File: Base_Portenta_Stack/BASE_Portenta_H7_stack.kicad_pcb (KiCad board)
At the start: 2 copper layers, 79.8 x 26.6 mm, 8 parts, among them J4 PinHeader_1x04_P2.00mm_Vertic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

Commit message: Updade
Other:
- outline, holes or cut-outs redrawn
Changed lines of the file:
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@@
       )
     )
-    (model "${KIPRJMOD}/Arduino-Portenta-H7-STEP-A210428.step"
+    (model "C:/Users/45262/Documents/GitHub/MTBeDRIVE/img/DF40C(2.0)-80DS.stp"
+      (offset (xyz 0.1 15.9 0.5))
+      (scale (xyz 1 1 1))
+      (rotate (xyz 90 -180 90))
+    )
+    (model "C:/Users/45262/Documents/GitHub/MTBeDRIVE/img/DF40C(2.0)-80DS.stp"
+      (offset (xyz -0.1 -27.3 0.5))
+      (scale (xyz 1 1 1))
+      (rotate (xyz -90 0 90))
+    )
+    (model "C:/Users/45262/Desktop/NRF_HALLA/Arduino-Portenta-H7-STEP-A210428.step"
       (offset (xyz 0 0 2))
       (scale (xyz 1 1 1))
@@
     )
   )
-  (gr_rect (start 106.21 80.47) (end 185.98 107.09) (layer "Edge.Cuts") (width 0.05) (fill none))
+  (gr_arc (start 183.950563 80.472791) (mid 185.42 80.95) (end 185.960563 82.392791) (layer "Edge.Cuts") (width 0.05))
+  (gr_line (start 184.047772 107.093354) (end 108.22 107.09) (layer "Edge.Cuts") (width 0.1))
+  (gr_arc (start 185.967772 105.083354) (mid 185.490563 106.552791) (end 184.047772 107.093354) (layer "Edge.Cuts") (width 0.05))
+  (gr_arc (start 108.22 107.09) (mid 106.750563 106.612791) (end 106.21 105.17) (layer "Edge.Cuts") (width 0.05))
+  (gr_line (start 108.122791 80.469437) (end 183.950563 80.472791) (layer "Edge.Cuts") (width 0.1))
+  (gr_arc (start 106.202791 82.479437) (mid 106.68 81.01) (end 108.122791 80.469437) (layer "Edge.Cuts") (width 0.05))
+  (gr_line (start 106.21 105.17) (end 106.202791 82.479437) (layer "Edge.Cuts") (width 0.1))
+  (gr_line (start 185.960563 82.392791) (end 185.967772 105.083354) (layer "Edge.Cuts") (width 0.1))
 )

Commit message: Log
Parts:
- added REF**: VSON-10-1EP_3x3mm_P0.5mm_EP1.2x2mm, Package_SON:VSON-10-1EP_3x3mm_P0.5mm_EP1.2x2mm, B.Cu at (167.6, 93.7)
- added REF**: D_1206_3216Metric, Diode_SMD:D_1206_3216Metric, B.Cu at (175.8, 93.6)
- added REF**: C_0805_2012Metric, Capacitor_SMD:C_0805_2012Metric, B.Cu at (181.6, 100.1)
- added REF**: C_1210_3225Metric, Capacitor_SMD:C_1210_3225Metric, B.Cu at (181.3, 86.3)
- added REF**: MountingHole_3.2mm_M3, MountingHole:MountingHole_3.2mm_M3, F.Cu at (182.2, 93.4)
- added REF**: MountingHole_3.2mm_M3, MountingHole:MountingHole_3.2mm_M3, F.Cu at (110.4, 93.4)
- added REF**: C_0805_2012Metric, Capacitor_SMD:C_0805_2012Metric, B.Cu at (171.4, 93.7)
- added REF**: SRP5050, MAX40056FAWA&plus_:SRP5050, B.Cu at (176.1, 98.1)
- added REF**: SOIC-8_EP_MNP, MP9486AGN-Z:MP9486AGN-Z, B.Cu at (176.1, 88.2)
- added REF**: C_1210_3225Metric, Capacitor_SMD:C_1210_3225Metric, B.Cu at (181.3, 82.9)
- added REF**: CP_EIA-7343-15_Kemet-W, Capacitor_Tantalum_SMD:CP_EIA-7343-15_Kemet-W, B.Cu at (178.7, 103.9)
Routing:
- added copper zone on B.Cu, net GND
- added copper zone on B.Cu, net SW
- added copper zone on B.Cu, net SWT_OUT_12V
- added copper zone on B.Cu, net VIN

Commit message: Update BASE_Portenta_H7_stack.kicad_pcb
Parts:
- removed the REF** at (110.4, 93.4)
- added REF**: PinHeader_1x04_P2.54mm_Vertical, Connector_PinHeader_2.54mm:PinHeader_1x04_P2.54mm_Vertical, F.Cu at (100.9, 97.5)
- added REF**: R_0603_1608Metric, Resistor_SMD:R_0603_1608Metric, B.Cu at (173.9, 82.0)
- added REF**: R_0603_1608Metric, Resistor_SMD:R_0603_1608Metric, B.Cu at (175.4, 82.0)
- added REF**: C_0603_1608Metric, Capacitor_SMD:C_0603_1608Metric, B.Cu at (176.9, 82.0)
- added REF**: PinHeader_1x06_P2.00mm_Vertical, Connector_PinHeader_2.00mm:PinHeader_1x06_P2.00mm_Vertical, F.Cu at (100.8, 82.5)
- REF**: moved to F.Cu
- U1: renamed from REF**; value MODULE_ABX00042 -> ABX00042
- moved REF** 0.51 mm to (181.7, 86.7)
- moved REF** 0.32 mm to (181.6, 83.0)
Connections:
- U1 pad J1_1: (no net) -> unconnected-(U1-PadJ1_1)
- U1 pad J1_10: (no net) -> unconnected-(U1-PadJ1_10)
- U1 pad J1_11: (no net) -> unconnected-(U1-PadJ1_11)
- U1 pad J1_12: (no net) -> unconnected-(U1-PadJ1_12)
- U1 pad J1_13: (no net) -> unconnected-(U1-PadJ1_13)
- U1 pad J1_14: (no net) -> unconnected-(U1-PadJ1_14)
- U1 pad J1_15: (no net) -> unconnected-(U1-PadJ1_15)
- U1 pad J1_16: (no net) -> unconnected-(U1-PadJ1_16)
- U1 pad J1_17: (no net) -> unconnected-(U1-PadJ1_17)
- U1 pad J1_18: (no net) -> unconnected-(U1-PadJ1_18)
- U1 pad J1_19: (no net) -> unconnected-(U1-PadJ1_19)
- U1 pad J1_2: (no net) -> unconnected-(U1-PadJ1_2)
- U1 pad J1_20: (no net) -> unconnected-(U1-PadJ1_20)
- U1 pad J1_21: (no net) -> Net-(U1-PadJ1_21)
- U1 pad J1_22: (no net) -> Net-(U1-PadJ1_22)
- U1 pad J1_23: (no net) -> unconnected-(U1-PadJ1_23)
- U1 pad J1_24: (no net) -> unconnected-(U1-PadJ1_24)
- U1 pad J1_25: (no net) -> unconnected-(U1-PadJ1_25)
- U1 pad J1_26: (no net) -> unconnected-(U1-PadJ1_26)
- U1 pad J1_27: (no net) -> unconnected-(U1-PadJ1_27)
- U1 pad J1_28: (no net) -> unconnected-(U1-PadJ1_28)
- U1 pad J1_29: (no net) -> unconnected-(U1-PadJ1_29)
- U1 pad J1_3: (no net) -> unconnected-(U1-PadJ1_3)
- U1 pad J1_30: (no net) -> unconnected-(U1-PadJ1_30)
- U1 pad J1_31: (no net) -> Net-(U1-PadJ1_22)
- U1 pad J1_32: (no net) -> Net-(U1-PadJ1_21)
- U1 pad J1_33: (no net) -> unconnected-(U1-PadJ1_33)
- U1 pad J1_34: (no net) -> unconnected-(U1-PadJ1_34)
- U1 pad J1_35: (no net) -> unconnected-(U1-PadJ1_35)
- U1 pad J1_36: (no net) -> unconnected-(U1-PadJ1_36)
- U1 pad J1_37: (no net) -> unconnected-(U1-PadJ1_37)
- U1 pad J1_38: (no net) -> unconnected-(U1-PadJ1_38)
- U1 pad J1_39: (no net) -> unconnected-(U1-PadJ1_39)
- U1 pad J1_4: (no net) -> unconnected-(U1-PadJ1_4)
- U1 pad J1_40: (no net) -> unconnected-(U1-PadJ1_40)
- U1 pad J1_41: (no net) -> Net-(U1-PadJ1_21)
- U1 pad J1_42: (no net) -> Net-(U1-PadJ1_22)
- U1 pad J1_43: (no net) -> unconnected-(U1-PadJ1_43)
- U1 pad J1_44: (no net) -> unconnected-(U1-PadJ1_44)
- U1 pad J1_45: (no net) -> unconnected-(U1-PadJ1_45)
- U1 pad J1_46: (no net) -> unconnected-(U1-PadJ1_46)
- U1 pad J1_47: (no net) -> Net-(U1-PadJ1_22)
- U1 pad J1_48: (no net) -> Net-(U1-PadJ1_21)
- U1 pad J1_49: (no net) -> unconnected-(U1-PadJ1_49)
- U1 pad J1_5: (no net) -> unconnected-(U1-PadJ1_5)
- U1 pad J1_50: (no net) -> unconnected-(U1-PadJ1_50)
- U1 pad J1_51: (no net) -> unconnected-(U1-PadJ1_51)
- U1 pad J1_52: (no net) -> unconnected-(U1-PadJ1_52)
- U1 pad J1_53: (no net) -> Net-(U1-PadJ1_53)
- U1 pad J1_54: (no net) -> Net-(U1-PadJ1_22)
- U1 pad J1_55: (no net) -> unconnected-(U1-PadJ1_55)
- U1 pad J1_56: (no net) -> unconnected-(U1-PadJ1_56)
- U1 pad J1_57: (no net) -> unconnected-(U1-PadJ1_57)
- U1 pad J1_58: (no net) -> unconnected-(U1-PadJ1_58)
- U1 pad J1_59: (no net) -> unconnected-(U1-PadJ1_59)
- U1 pad J1_6: (no net) -> unconnected-(U1-PadJ1_6)
- U1 pad J1_60: (no net) -> unconnected-(U1-PadJ1_60)
- U1 pad J1_61: (no net) -> unconnected-(U1-PadJ1_61)
- U1 pad J1_62: (no net) -> unconnected-(U1-PadJ1_62)
- U1 pad J1_63: (no net) -> unconnected-(U1-PadJ1_63)
- U1 pad J1_64: (no net) -> Net-(U1-PadJ1_53)
- U1 pad J1_65: (no net) -> unconnected-(U1-PadJ1_65)
- U1 pad J1_66: (no net) -> unconnected-(U1-PadJ1_66)
- U1 pad J1_67: (no net) -> unconnected-(U1-PadJ1_67)
- U1 pad J1_68: (no net) -> unconnected-(U1-PadJ1_68)
- U1 pad J1_69: (no net) -> unconnected-(U1-PadJ1_69)
- U1 pad J1_7: (no net) -> unconnected-(U1-PadJ1_7)
- U1 pad J1_70: (no net) -> unconnected-(U1-PadJ1_70)
- U1 pad J1_71: (no net) -> unconnected-(U1-PadJ1_71)
- U1 pad J1_72: (no net) -> unconnected-(U1-PadJ1_72)
- U1 pad J1_73: (no net) -> unconnected-(U1-PadJ1_73)
- U1 pad J1_74: (no net) -> unconnected-(U1-PadJ1_74)
- U1 pad J1_75: (no net) -> unconnected-(U1-PadJ1_75)
- U1 pad J1_76: (no net) -> unconnected-(U1-PadJ1_76)
- U1 pad J1_77: (no net) -> unconnected-(U1-PadJ1_77)
- U1 pad J1_78: (no net) -> unconnected-(U1-PadJ1_78)
- U1 pad J1_79: (no net) -> unconnected-(U1-PadJ1_79)
- U1 pad J1_8: (no net) -> unconnected-(U1-PadJ1_8)
- U1 pad J1_80: (no net) -> unconnected-(U1-PadJ1_80)
- U1 pad J1_9: (no net) -> unconnected-(U1-PadJ1_9)
- U1 pad J2_1: (no net) -> unconnected-(U1-PadJ2_1)
- U1 pad J2_10: (no net) -> unconnected-(U1-PadJ2_10)
- U1 pad J2_11: (no net) -> unconnected-(U1-PadJ2_11)
- U1 pad J2_12: (no net) -> unconnected-(U1-PadJ2_12)
- U1 pad J2_13: (no net) -> unconnected-(U1-PadJ2_13)
- U1 pad J2_14: (no net) -> unconnected-(U1-PadJ2_14)
- U1 pad J2_15: (no net) -> unconnected-(U1-PadJ2_15)
- U1 pad J2_16: (no net) -> unconnected-(U1-PadJ2_16)
- U1 pad J2_17: (no net) -> unconnected-(U1-PadJ2_17)
- U1 pad J2_18: (no net) -> unconnected-(U1-PadJ2_18)
- U1 pad J2_19: (no net) -> unconnected-(U1-PadJ2_19)
- U1 pad J2_2: (no net) -> unconnected-(U1-PadJ2_2)
- U1 pad J2_20: (no net) -> unconnected-(U1-PadJ2_20)
- U1 pad J2_21: (no net) -> unconnected-(U1-PadJ2_21)
- U1 pad J2_22: (no net) -> unconnected-(U1-PadJ2_22)
- U1 pad J2_23: (no net) -> Net-(U1-PadJ2_23)
- U1 pad J2_24: (no net) -> Net-(U1-PadJ2_24)
- U1 pad J2_25: (no net) -> unconnected-(U1-PadJ2_25)
- U1 pad J2_26: (no net) -> unconnected-(U1-PadJ2_26)
- U1 pad J2_27: (no net) -> unconnected-(U1-PadJ2_27)
- U1 pad J2_28: (no net) -> unconnected-(U1-PadJ2_28)
- U1 pad J2_29: (no net) -> unconnected-(U1-PadJ2_29)
- U1 pad J2_3: (no net) -> unconnected-(U1-PadJ2_3)
- U1 pad J2_30: (no net) -> unconnected-(U1-PadJ2_30)
- U1 pad J2_31: (no net) -> unconnected-(U1-PadJ2_31)
- U1 pad J2_32: (no net) -> unconnected-(U1-PadJ2_32)
- U1 pad J2_33: (no net) -> Net-(U1-PadJ2_24)
- U1 pad J2_34: (no net) -> unconnected-(U1-PadJ2_34)
- U1 pad J2_35: (no net) -> unconnected-(U1-PadJ2_35)
- U1 pad J2_36: (no net) -> unconnected-(U1-PadJ2_36)
- U1 pad J2_37: (no net) -> unconnected-(U1-PadJ2_37)
- U1 pad J2_38: (no net) -> unconnected-(U1-PadJ2_38)
- U1 pad J2_39: (no net) -> unconnected-(U1-PadJ2_39)
- U1 pad J2_4: (no net) -> unconnected-(U1-PadJ2_4)
- U1 pad J2_40: (no net) -> unconnected-(U1-PadJ2_40)
- U1 pad J2_41: (no net) -> unconnected-(U1-PadJ2_41)
- U1 pad J2_42: (no net) -> unconnected-(U1-PadJ2_42)
- U1 pad J2_43: (no net) -> Net-(U1-PadJ2_23)
- U1 pad J2_44: (no net) -> Net-(U1-PadJ2_24)
- U1 pad J2_45: (no net) -> unconnected-(U1-PadJ2_45)
- U1 pad J2_46: (no net) -> unconnected-(U1-PadJ2_46)
- U1 pad J2_47: (no net) -> unconnected-(U1-PadJ2_47)
- U1 pad J2_48: (no net) -> unconnected-(U1-PadJ2_48)
- U1 pad J2_49: (no net) -> unconnected-(U1-PadJ2_49)
- U1 pad J2_5: (no net) -> unconnected-(U1-PadJ2_5)
- U1 pad J2_50: (no net) -> unconnected-(U1-PadJ2_50)
- U1 pad J2_51: (no net) -> unconnected-(U1-PadJ2_51)
- U1 pad J2_52: (no net) -> unconnected-(U1-PadJ2_52)
- U1 pad J2_53: (no net) -> unconnected-(U1-PadJ2_53)
- U1 pad J2_54: (no net) -> unconnected-(U1-PadJ2_54)
- U1 pad J2_55: (no net) -> unconnected-(U1-PadJ2_55)
- U1 pad J2_56: (no net) -> unconnected-(U1-PadJ2_56)
- U1 pad J2_57: (no net) -> Net-(U1-PadJ2_24)
- U1 pad J2_58: (no net) -> unconnected-(U1-PadJ2_58)
- U1 pad J2_59: (no net) -> unconnected-(U1-PadJ2_59)
- U1 pad J2_6: (no net) -> unconnected-(U1-PadJ2_6)
- U1 pad J2_60: (no net) -> unconnected-(U1-PadJ2_60)
- U1 pad J2_61: (no net) -> unconnected-(U1-PadJ2_61)
- U1 pad J2_62: (no net) -> unconnected-(U1-PadJ2_62)
- U1 pad J2_63: (no net) -> unconnected-(U1-PadJ2_63)
- U1 pad J2_64: (no net) -> unconnected-(U1-PadJ2_64)
- U1 pad J2_65: (no net) -> unconnected-(U1-PadJ2_65)
- U1 pad J2_66: (no net) -> unconnected-(U1-PadJ2_66)
- U1 pad J2_67: (no net) -> unconnected-(U1-PadJ2_67)
- U1 pad J2_68: (no net) -> unconnected-(U1-PadJ2_68)
- U1 pad J2_69: (no net) -> Net-(U1-PadJ2_23)
- U1 pad J2_7: (no net) -> unconnected-(U1-PadJ2_7)
- U1 pad J2_70: (no net) -> Net-(U1-PadJ2_24)
- U1 pad J2_71: (no net) -> unconnected-(U1-PadJ2_71)
- U1 pad J2_72: (no net) -> unconnected-(U1-PadJ2_72)
- U1 pad J2_73: (no net) -> unconnected-(U1-PadJ2_73)
- U1 pad J2_74: (no net) -> unconnected-(U1-PadJ2_74)
- U1 pad J2_75: (no net) -> unconnected-(U1-PadJ2_75)
- U1 pad J2_76: (no net) -> unconnected-(U1-PadJ2_76)
- U1 pad J2_77: (no net) -> unconnected-(U1-PadJ2_77)
- U1 pad J2_78: (no net) -> unconnected-(U1-PadJ2_78)
- U1 pad J2_79: (no net) -> unconnected-(U1-PadJ2_79)
- U1 pad J2_8: (no net) -> unconnected-(U1-PadJ2_8)
- U1 pad J2_80: (no net) -> unconnected-(U1-PadJ2_80)
- U1 pad J2_9: (no net) -> unconnected-(U1-PadJ2_9)
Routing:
- net SWT_OUT_12V: vias 0 -> 9
- added copper zone on F.Cu, net SWT_OUT_12V
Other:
- board size 79.8 x 26.6 mm -> 87.5 x 26.7 mm
- board text added: "+"
- board text added: "-"
- board text added: "12V"
- board text added: "CAN"
- board text added: "GND"
- board text added: "HALL"

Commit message: Log
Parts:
- moved REF** 0.55 mm to (100.3, 97.5)
- moved REF** 0.55 mm to (100.3, 82.5)
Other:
- outline, holes or cut-outs redrawn
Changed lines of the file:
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@@
   (net 157 "unconnected-(U1-PadJ2_80)")
   (footprint "Connector_PinHeader_2.54mm:PinHeader_1x04_P2.54mm_Vertical" (layer "F.Cu")
-    (at 100.9 97.5)
+    (at 100.35 97.5)
     (descr "Through hole straight pin header, 1x04, 2.54mm pitch, single row")
     (tags "Through hole pin header THT 1x04 2.54mm single row")
     (attr through_hole)
-    (fp_text reference "REF**" (at 0 -2.33) (layer "F.SilkS")
+    (fp_text reference "REF**" (at 0 -2.33) (layer "F.SilkS") hide
       (effects (font (size 1 1) (thickness 0.15)))
     )
-    (fp_text value "PinHeader_1x04_P2.54mm_Vertical" (at 0 9.95) (layer "F.Fab")
+    (fp_text value "PinHeader_1x04_P2.54mm_Vertical" (at 0 9.95) (layer "F.Fab") hide
       (effects (font (size 1 1) (thickness 0.15)))
     )
-    (fp_text user "${REFERENCE}" (at 0 3.81 90) (layer "F.Fab")
+    (fp_text user "${REFERENCE}" (at 0 3.81 90) (layer "F.Fab") hide
       (effects (font (size 1 1) (thickness 0.15)))
     )
@@
     (pad "4" thru_hole oval (at 0 7.62) (size 1.7 1.7) (drill 1) (layers *.Cu *.Mask)
       (net 11 "SWT_OUT_12V"))
-    (model "${KICAD6_3DMODEL_DIR}/Connector_PinHeader_2.54mm.3dshapes/PinHeader_1x04_P2.54mm_Vertical.wrl"
+    (model "${KICAD6_3DMODEL_DIR}/Connector_PinHeader_2.54mm.3dshapes/PinHeader_1x04_P2.54mm_Vertical.wrl" hide
       (offset (xyz 0 0 0))
       (scale (xyz 1 1 1))
@@
   )
   (footprint "Connector_PinHeader_2.00mm:PinHeader_1x06_P2.00mm_Vertical" (layer "F.Cu")
-    (at 100.85 82.55)
+    (at 100.3 82.55)
     (descr "Through hole straight pin header, 1x06, 2.00mm pitch, single row")
     (tags "Through hole pin header THT 1x06 2.00mm single row")
     (attr through_hole)
-    (fp_text reference "REF**" (at 0 -2.06) (layer "F.SilkS")
+    (fp_text reference "REF**" (at 0 -2.06) (layer "F.SilkS") hide
       (effects (font (size 1 1) (thickness 0.15)))
     )
-    (fp_text value "PinHeader_1x06_P2.00mm_Vertical" (at 0 12.06) (layer "F.Fab")
+    (fp_text value "PinHeader_1x06_P2.00mm_Vertical" (at 0 12.06) (layer "F.Fab") hide
       (effects (font (size 1 1) (thickness 0.15)))
     )
-    (fp_text user "${REFERENCE}" (at 0 5 90) (layer "F.Fab")
+    (fp_text user "${REFERENCE}" (at 0 5 90) (layer "F.Fab") hide
       (effects (font (size 1 1) (thickness 0.15)))
     )
@@
     (pad "5" thru_hole oval (at 0 8) (size 1.35 1.35) (drill 0.8) (layers *.Cu *.Mask))
     (pad "6" thru_hole oval (at 0 10) (size 1.35 1.35) (drill 0.8) (layers *.Cu *.Mask))
-    (model "${KICAD6_3DMODEL_DIR}/Connector_PinHeader_2.00mm.3dshapes/PinHeader_1x06_P2.00mm_Vertical.wrl"
+    (model "${KICAD6_3DMODEL_DIR}/Connector_PinHeader_2.00mm.3dshapes/PinHeader_1x06_P2.00mm_Vertical.wrl" hide
       (offset (xyz 0 0 0))
       (scale (xyz 1 1 1))
@@
   )
   (gr_arc (start 182.41 80.472791) (mid 183.879437 80.95) (end 184.42 82.392791) (layer "Edge.Cuts") (width 0.05))
-  (gr_line (start 182.557209 107.093354) (end 99 107.05) (layer "Edge.Cuts") (width 0.1))
+  (gr_line (start 182.507209 107.093354) (end 99 107.05) (layer "Edge.Cuts") (width 0.1))
   (gr_arc (start 184.427209 105.083354) (mid 183.95 106.552791) (end 182.507209 107.093354) (layer "Edge.Cuts") (width 0.05))
   (gr_arc (start 99 107.05) (mid 97.530563 106.572791) (end 96.99 105.13) (layer "Edge.Cuts") (width 0.05))
@@
   (gr_line (start 96.99 105.13) (end 96.982791 82.439437) (layer "Edge.Cuts") (width 0.1))
   (gr_line (start 184.42 82.392791) (end 184.427209 105.083354) (layer "Edge.Cuts") (width 0.1))
-  (gr_text "+" (at 97.9 102.55 90) (layer "F.SilkS")
+  (gr_text "+" (at 97.6 102.55 90) (layer "F.SilkS")
     (effects (font (size 1 1) (thickness 0.2)))
   )
-  (gr_text "-" (at 97.9 100.25 90) (layer "F.SilkS")
+  (gr_text "-" (at 97.6 100.25 90) (layer "F.SilkS")
     (effects (font (size 1 1) (thickness 0.2)))
   )
@@
     (effects (font (size 3 3) (thickness 0.75)))
   )
-  (gr_text "GND" (at 98.1 97.35 90) (layer "F.SilkS")
+  (gr_text "GND" (at 97.7 97.2 90) (layer "F.SilkS")
     (effects (font (size 1 1) (thickness 0.2)))
   )
@@
     (effects (font (size 3 3) (thickness 0.75)))
   )
-  (gr_text "12V" (at 98.1 105.35 90) (layer "F.SilkS")
+  (gr_text "12V" (at 97.7 105.2 90) (layer "F.SilkS")
     (effects (font (size 1 1) (thickness 0.2)))
   )

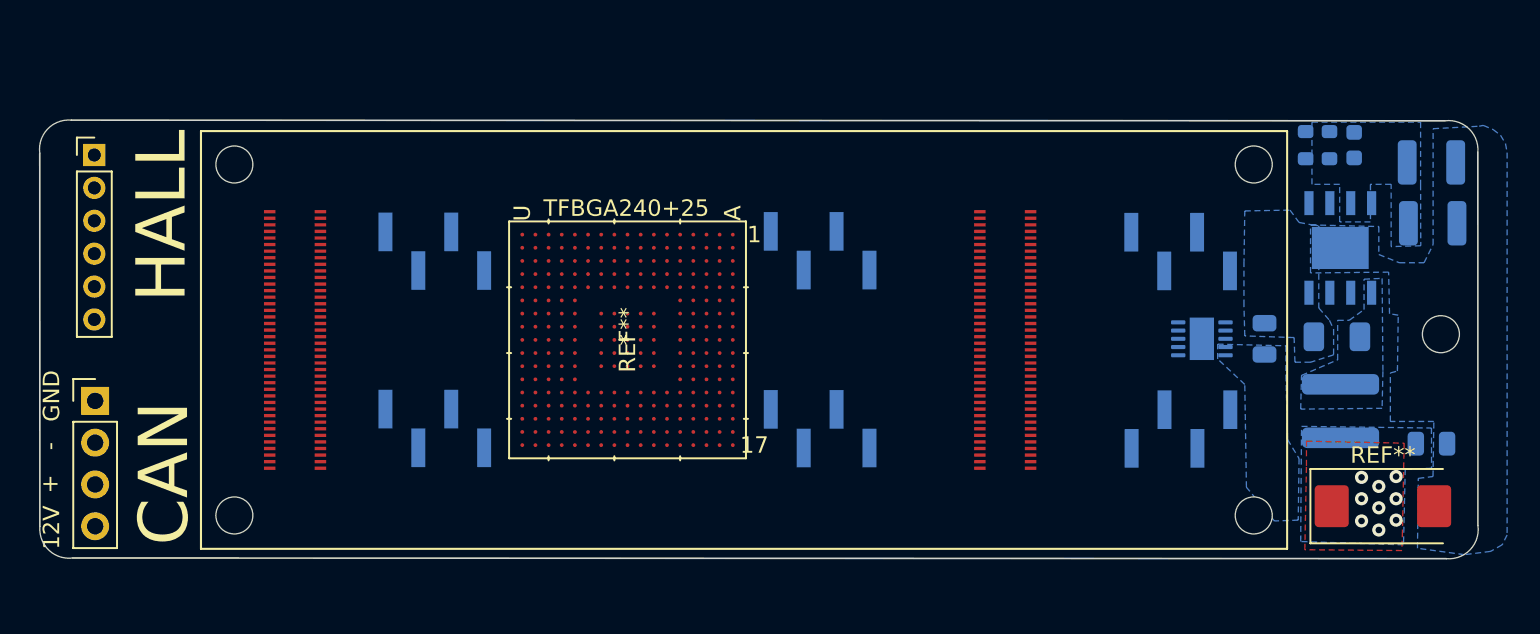
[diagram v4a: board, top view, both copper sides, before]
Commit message: Moved Portenta for CAN and Hall wire
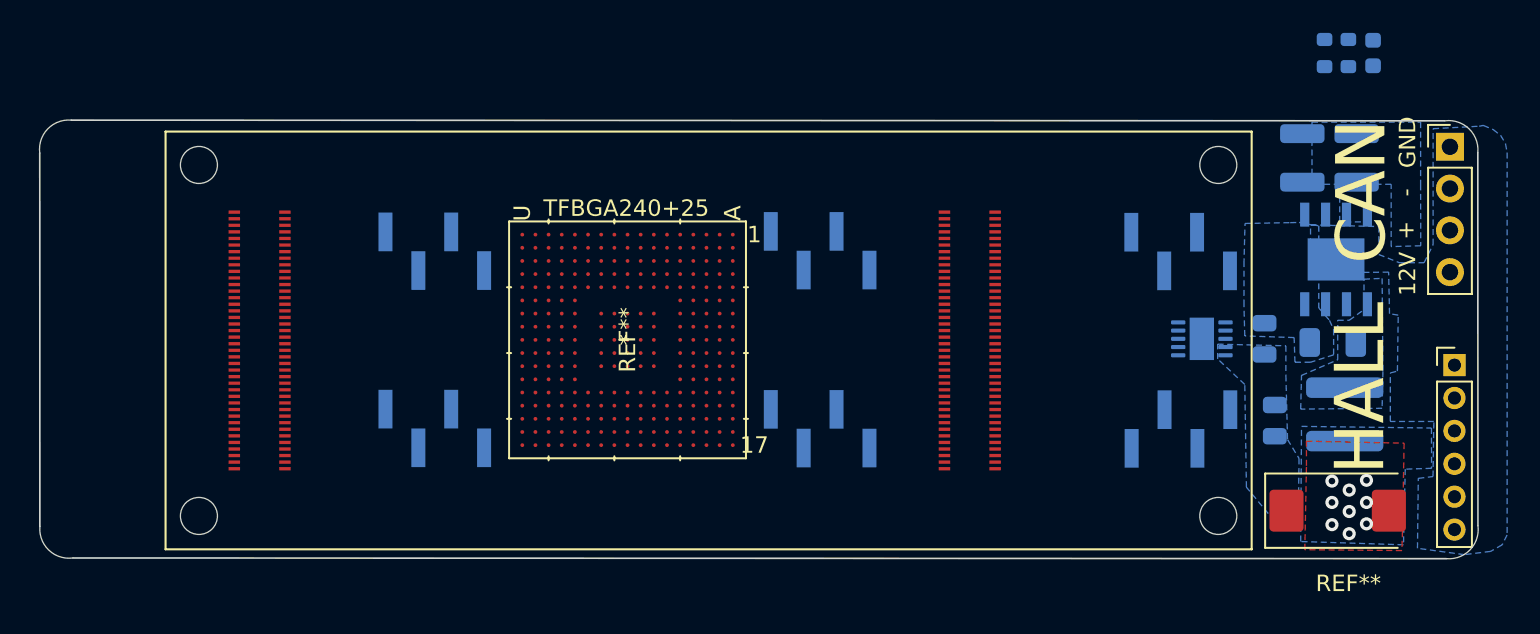
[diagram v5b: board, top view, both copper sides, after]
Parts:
- removed the REF** at (182.2, 93.4)
- moved REF** 83.8 mm to (182.7, 82.0)
- moved REF** 83.7 mm to (183.0, 95.3)
- moved REF** 9.63 mm to (172.1, 98.7), turned to -90 degrees
- moved REF** 7.85 mm to (173.8, 82.7), turned to -90 degrees
- moved REF** 6.10 mm to (177.1, 82.7), turned to -90 degrees
- moved REF** 5.72 mm to (176.6, 76.3)
- moved REF** 5.72 mm to (178.1, 76.3)
- moved REF** 5.72 mm to (175.1, 76.3)
- moved REF** 2.76 mm to (175.9, 104.2)
- moved U1 2.16 mm to (137.7, 93.8)
- moved REF** 0.75 mm to (175.8, 88.9)
- moved REF** 0.43 mm to (175.6, 94.0)
- moved REF** 0.32 mm to (176.3, 98.3)

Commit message: Changelog
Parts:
- added REF**: PinHeader_1x12_P2.00mm_Vertical, Connector_PinHeader_2.00mm:PinHeader_1x12_P2.00mm_Vertical, F.Cu at (101.6, 82.7)
- moved REF** 14.2 mm to (172.5, 90.3), turned to 0 degrees
- moved REF** 13.1 mm to (172.5, 88.8), turned to 0 degrees
- moved REF** 12.3 mm to (172.5, 87.3), turned to 180 degrees
- moved REF** 1.07 mm to (176.9, 88.9)
- moved REF** 0.33 mm to (175.6, 104.2), turned to 180 degrees
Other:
- board size 87.5 x 26.7 mm -> 84.2 x 26.7 mm

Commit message: Aligned
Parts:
- removed the REF** at (101.6, 82.7)
- moved J4 2.34 mm to (164.0, 88.4)
- moved J4 2.34 mm to (164.0, 99.2)
- moved REF** 2.34 mm to (165.3, 93.7)
- moved U1 0.54 mm to (137.1, 93.8)
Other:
- board size 84.2 x 26.7 mm -> 82.1 x 26.7 mm

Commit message: Log
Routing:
- removed copper zone on B.Cu, net VIN
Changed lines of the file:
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@@
     (polygon
       (pts
-        (xy 178.65 95.7)
-        (xy 178.6 97.95)
-        (xy 173.65 98)
-        (xy 173.7 95.95)
-        (xy 175.9 95)
-        (xy 175.9 92.6)
-        (xy 176.6 92.6)
-        (xy 177.5 91.95)
-        (xy 177.5 90.1)
-        (xy 178.6 90.05)
+        (xy 179.687647 98.195301)
+        (xy 173.89 98.22)
+        (xy 173.91 96.06)
+        (xy 176.427647 95.245301)
+        (xy 176.427647 92.845301)
+        (xy 177.127647 92.845301)
+        (xy 178.027647 92.809284)
+        (xy 178.030674 90.445813)
+        (xy 179.690674 90.395813)
       )
     )
@@
       )
     )
-  )
-  (zone (net 1) (net_name "VIN") (layer "B.Cu") (hatch edge 0.508)
-    (connect_pads yes (clearance 0.508))
-    (min_thickness 0.254) (filled_areas_thickness no)
-    (fill yes (thermal_gap 0.508) (thermal_bridge_width 0.508))
-    (polygon
-      (pts
-        (xy 180.94 84.332)
-        (xy 180.95 88.068)
-        (xy 179.15 88.118)
-        (xy 179.15 84.332)
-        (xy 177.892 84.332)
-        (xy 177.892 86.618)
-        (xy 176.022 86.618)
-        (xy 176.022 84.332)
-        (xy 174.336 84.332)
-        (xy 174.336 80.55)
-        (xy 180.94 80.55)
-      )
-    )
-  )
-  (zone (net 6) (net_name "GND") (layer "B.Cu") (hatch edge 0.508)
-    (connect_pads yes (clearance 0.508))
-    (min_thickness 0.254) (filled_areas_thickness no)
-    (fill yes (thermal_gap 0.508) (thermal_bridge_width 0.508))
-    (polygon
-      (pts
-        (xy 185.35 81)
-        (xy 185.8 81.35)
-        (xy 186.1 81.85)
-        (xy 186.2 82.4)
-        (xy 186.2 105.65)
-        (xy 185.9 106.25)
-        (xy 185.2 106.65)
-        (xy 183.6 106.85)
-        (xy 180.749874 106.460587)
-        (xy 180.799874 102.210587)
-        (xy 181.69535 102.09822)
-        (xy 181.745338 98.75)
-        (xy 179.099988 98.750636)
-        (xy 179.1 95.800636)
-        (xy 179.530342 95.687848)
-        (xy 179.580342 92.287848)
-        (xy 179.050022 92.201056)
-        (xy 178.996589 89.671403)
-        (xy 174.246567 89.720347)
-        (xy 174.25 86.8)
-        (xy 178.4 86.9)
-        (xy 178.4 88.6)
-        (xy 179.65 89.1)
-        (xy 181.15 89.1)
-        (xy 181.7 88)
-        (xy 181.7 80.95)
-        (xy 184.5 80.8)
-        (xy 184.75 80.75)
-      )
-    )
